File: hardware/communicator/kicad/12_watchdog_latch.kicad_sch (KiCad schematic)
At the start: 8 parts, among them U30 TPS3431SDRBR, U31 SN74LVC1G11DCKR, U32 SN74LVC1G74DCUR

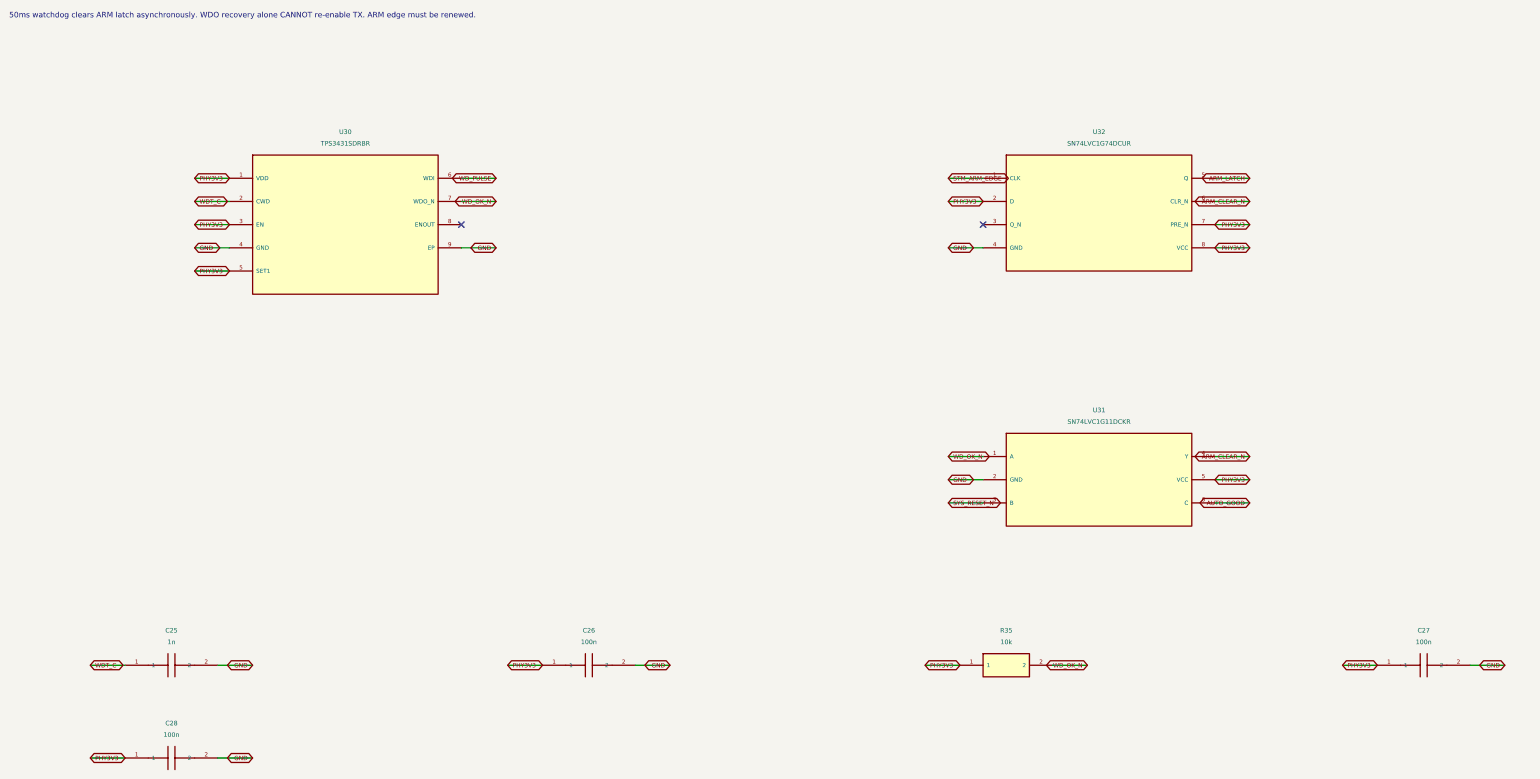
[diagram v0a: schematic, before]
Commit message: feat: add R1 detailed hardware and navigation protocol review candidate
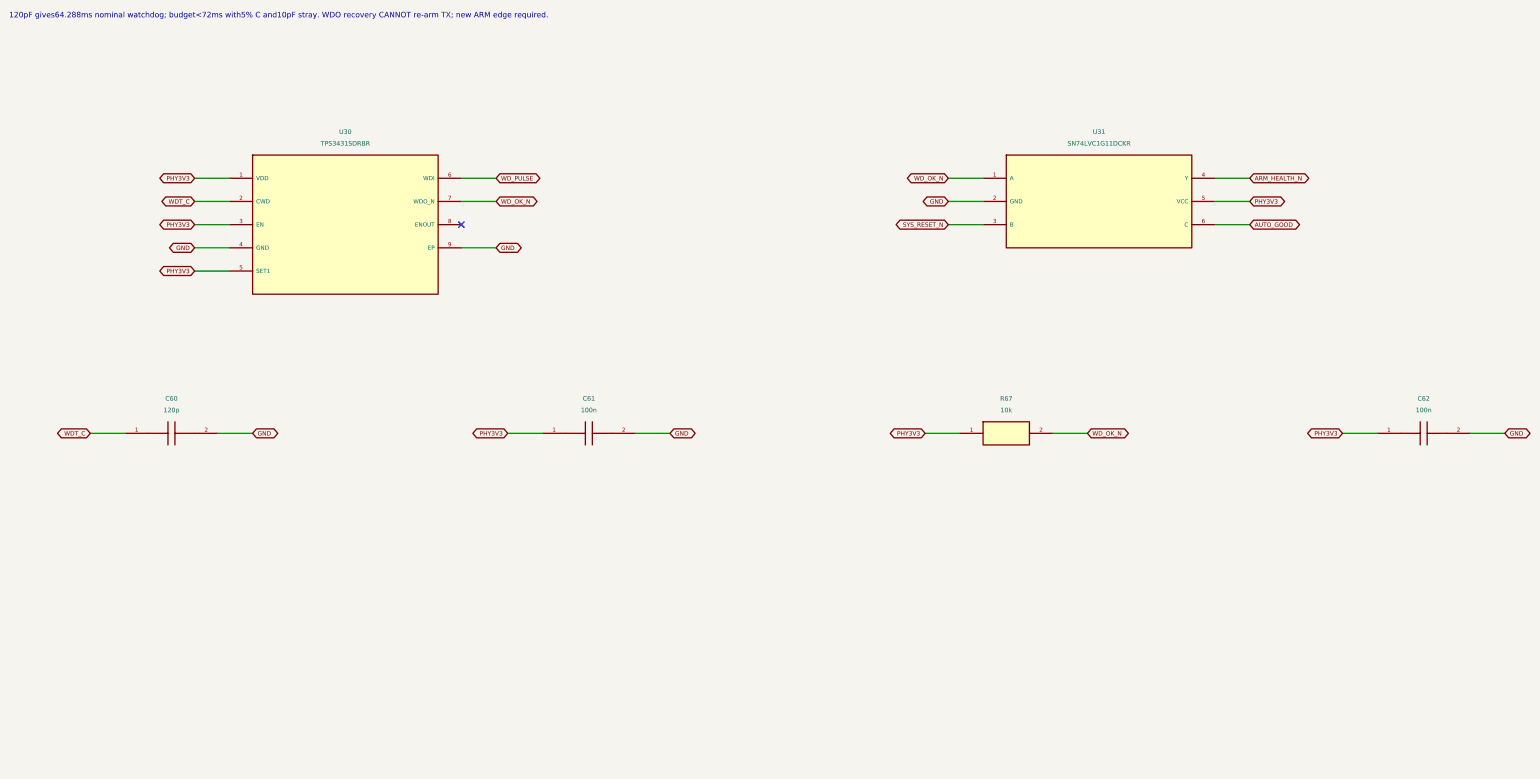
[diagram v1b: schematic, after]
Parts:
- removed C25: 1n, CANView:Capacitor_SMD__C_0402_1005Metric, symbol CANView:CANView_communicator_C25
- removed C26: 100n, CANView:Capacitor_SMD__C_0402_1005Metric, symbol CANView:CANView_communicator_C26
- removed C27: 100n, CANView:Capacitor_SMD__C_0402_1005Metric, symbol CANView:CANView_communicator_C27
- removed C28: 100n, CANView:Capacitor_SMD__C_0402_1005Metric, symbol CANView:CANView_communicator_C28
- removed R35: 10k, CANView:Resistor_SMD__R_0402_1005Metric, symbol CANView:CANView_communicator_R35
- removed U32: SN74LVC1G74DCUR, CANView:Package_SO__VSSOP-8_2.3x2mm_P0.5mm, symbol CANView:CANView_communicator_U32
- added C60: 120p, CANView:Capacitor_SMD__C_0402_1005Metric, symbol CANView:CANView_communicator_C60
- added C61: 100n, CANView:Capacitor_SMD__C_0402_1005Metric, symbol CANView:CANView_communicator_C61
- added C62: 100n, CANView:Capacitor_SMD__C_0402_1005Metric, symbol CANView:CANView_communicator_C62
- added R67: 10k, CANView:Resistor_SMD__R_0402_1005Metric, symbol CANView:CANView_communicator_R67
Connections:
- net GND: now also C60.2, C61.2, C62.2
- net PHY3V3: now also C61.1, C62.1, R67.1
- net WDT_C: now also C60.1
- net WD_OK_N: now also R67.2
- net ARM_CLEAR_N renamed ARM_HEALTH_N
- no-connect marks 2 -> 1
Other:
- note added: "120pF gives64.288ms nominal watchdog; budget<72ms with5% C and10pF stray. WDO recovery CANNOT re-arm TX; new ARM edge required."
- note removed: "50ms watchdog clears ARM latch asynchronously. WDO recovery alone CANNOT re-enable TX. ARM edge must be renewed."
- moved on the sheet: U31

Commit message: fix: close hardware rail-fault paths and sensor contract gaps
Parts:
- removed C60: 120p, CANView:Capacitor_SMD__C_0402_1005Metric, symbol CANView:CANView_communicator_C60
- removed C61: 100n, CANView:Capacitor_SMD__C_0402_1005Metric, symbol CANView:CANView_communicator_C61
- removed R67: 10k, CANView:Resistor_SMD__R_0402_1005Metric, symbol CANView:CANView_communicator_R67
- added C63: 100n, CANView:Capacitor_SMD__C_0402_1005Metric, symbol CANView:CANView_communicator_C63
- added C64: 100n, CANView:Capacitor_SMD__C_0402_1005Metric, symbol CANView:CANView_communicator_C64
- added R70: 10k, CANView:Resistor_SMD__R_0402_1005Metric, symbol CANView:CANView_communicator_R70
- C62: value 100n -> 120p; MPN GEN-C-0402-100n-16V-X7R -> GEN-C-0402-120p-16V-C0G; Specification 16V; ±10%; X7R; -55..125C; verify effective capacitance und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 -> 16V; ±5%; C0G; -55..125C; verify effective capacitance unde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
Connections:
- net GND: now also C63.2, C64.2
- net PHY3V3: now also C63.1, C64.1, R70.1; no longer C62.1
- net WDT_C: now also C62.1
- net WD_OK_N: now also R70.2
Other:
- moved on the sheet: C62

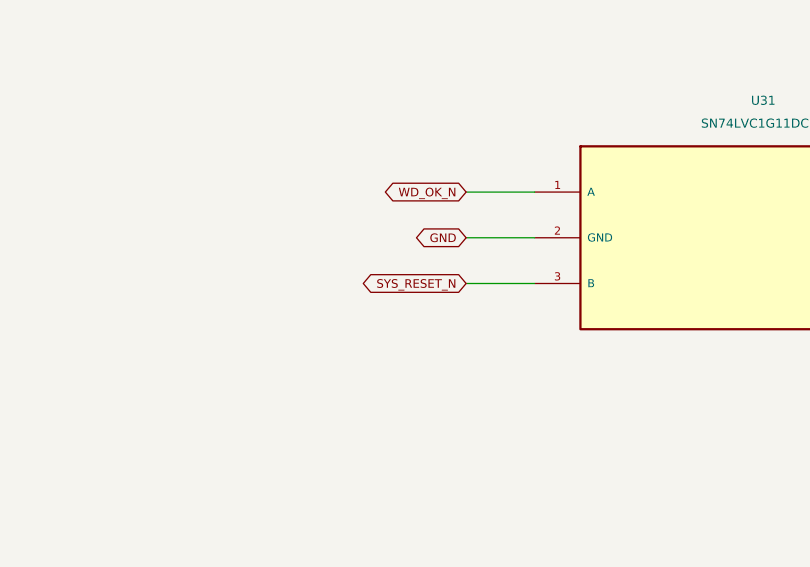
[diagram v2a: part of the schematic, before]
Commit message: Design independent OTA recovery and update N16R8 hardware
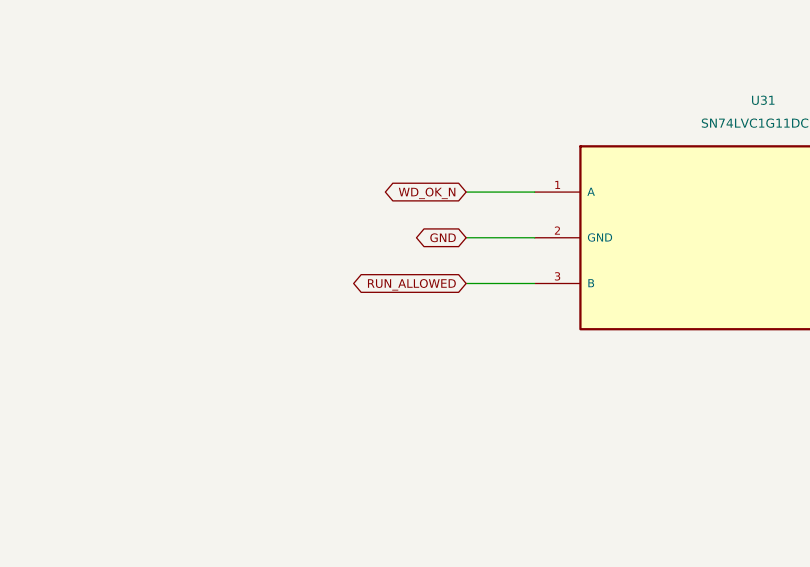
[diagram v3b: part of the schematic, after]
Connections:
- net SYS_RESET_N renamed RUN_ALLOWED
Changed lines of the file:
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@@
 (global_label "GND" (shape bidirectional) (at 220.9800 55.8800 180) (effects (font (size 0.95 0.95)) (justify right)) (property "Intersheetrefs" "${INTERSHEET_REFS}" (at 220.9800 55.8800 0) (hide yes) (effects (font (size 1.0 1.0)) )))
 (wire (pts (xy 228.6000 60.9600) (xy 220.9800 60.9600)) (stroke (width 0) (type default)))
-(global_label "SYS_RESET_N" (shape bidirectional) (at 220.9800 60.9600 180) (effects (font (size 0.95 0.95)) (justify right)) (property "Intersheetrefs" "${INTERSHEET_REFS}" (at 220.9800 60.9600 0) (hide yes) (effects (font (size 1.0 1.0)) )))
+(global_label "RUN_ALLOWED" (shape bidirectional) (at 220.9800 60.9600 180) (effects (font (size 0.95 0.95)) (justify right)) (property "Intersheetrefs" "${INTERSHEET_REFS}" (at 220.9800 60.9600 0) (hide yes) (effects (font (size 1.0 1.0)) )))
 (wire (pts (xy 279.4000 50.8000) (xy 287.0200 50.8000)) (stroke (width 0) (type default)))
 (global_label "ARM_HEALTH_N" (shape bidirectional) (at 287.0200 50.8000 0) (effects (font (size 0.95 0.95)) (justify left)) (property "Intersheetrefs" "${INTERSHEET_REFS}" (at 287.0200 50.8000 0) (hide yes) (effects (font (size 1.0 1.0)) )))
